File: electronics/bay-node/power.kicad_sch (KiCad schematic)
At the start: 26 parts, among them J1 24V IN, J2 24V OUT, Q1 SUD50P06-15, U1 TPS54360BDDAR, U2 AMS1117-3.3

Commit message: BOM: bulk hardware prices, JLC PCBA type per board
- hardware at bulk prices (T-nuts, screws, heat-set inserts, corner
  brackets), generic USB-C panel extensions; drop the label tape (the
  printed bay_label fills the drawer recess); heat-set inserts for camera
  pods only where a camera hangs
- catalog: standard_only flag (ESP32-S3-MINI-1, WS2812B-2020 cannot be
  placed with JLC Economic PCBA); bom.py prices Standard PCBA for the
  bay node and Economic for the power hub
- electrolytics moved to the Economic-capable LCSC listings of the same
  parts (C3352, C3358); PCB footprint fields synced, ERC/DRC/parity clean
- docs: JLC assembly notes (no Basic drop-ins for the extended parts)

Total ~EUR 927 -> ~EUR 828 (EUR 66 -> 59 per bay).

Co-Authored-By: Claude Opus 5.5 <noreply@anthropic.com>
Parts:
- C1: LCSC C72480 -> C3352; Manufacturer ROQANG -> Honor Elec
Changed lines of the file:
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@@
 			)
 		)
-		(property "Manufacturer" "ROQANG"
+		(property "Manufacturer" "Honor Elec"
 			(at 229.87 49.53 0)
 			(effects
@@
 			)
 		)
-		(property "LCSC" "C72480"
+		(property "LCSC" "C3352"
 			(at 229.87 49.53 0)
 			(effects

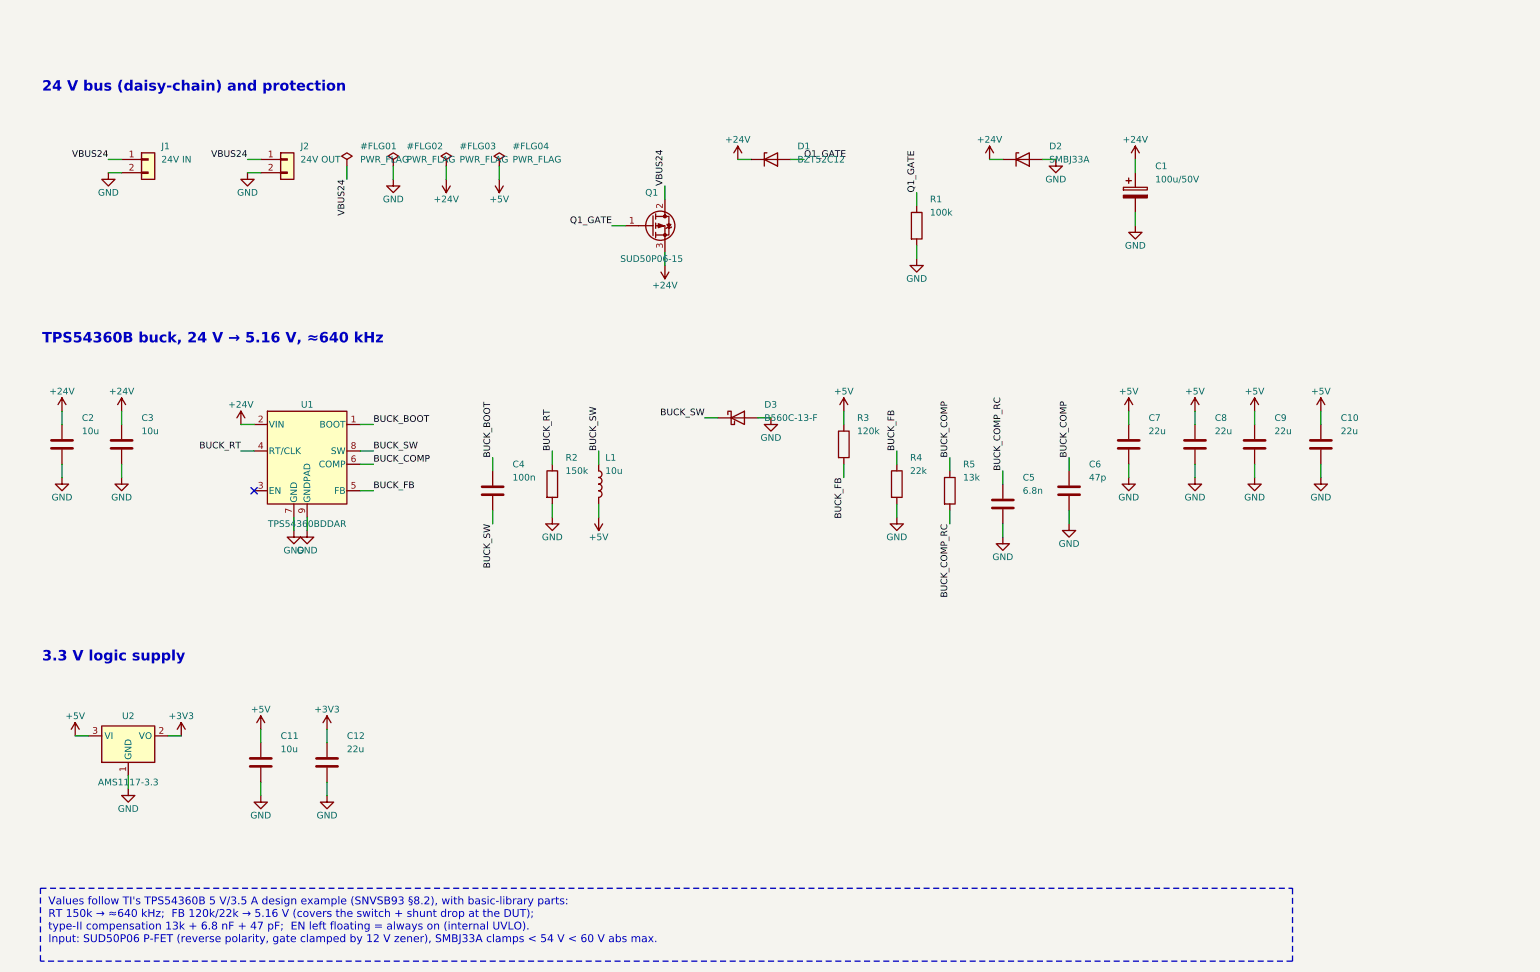
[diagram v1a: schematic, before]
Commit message: Schematics: draw real wires and an overview block diagram
The generator used to connect every pin through a net label only. Now,
in each block, the part with the most pins is the anchor and the
two-pin parts that share a signal with one of its side pins hang off
that pin on a real wire; parts chained behind them (R -> C -> GND)
stack underneath, and anchor-less blocks (pull-ups, reset/boot
buttons) are adopted by the anchor they connect to. Power symbols on
side pins point outward; power-flag references are hidden.

The root sheet becomes a block diagram: the supply rails each sheet
uses across the top, and one lane per pair of sheets listing the
signals they share.

Every wired net still carries one label, so net names, ERC (0) and the
PCB's schematic parity (0) are unchanged; the routed PCBs are untouched.

Co-Authored-By: Claude Opus 5.5 <noreply@anthropic.com>
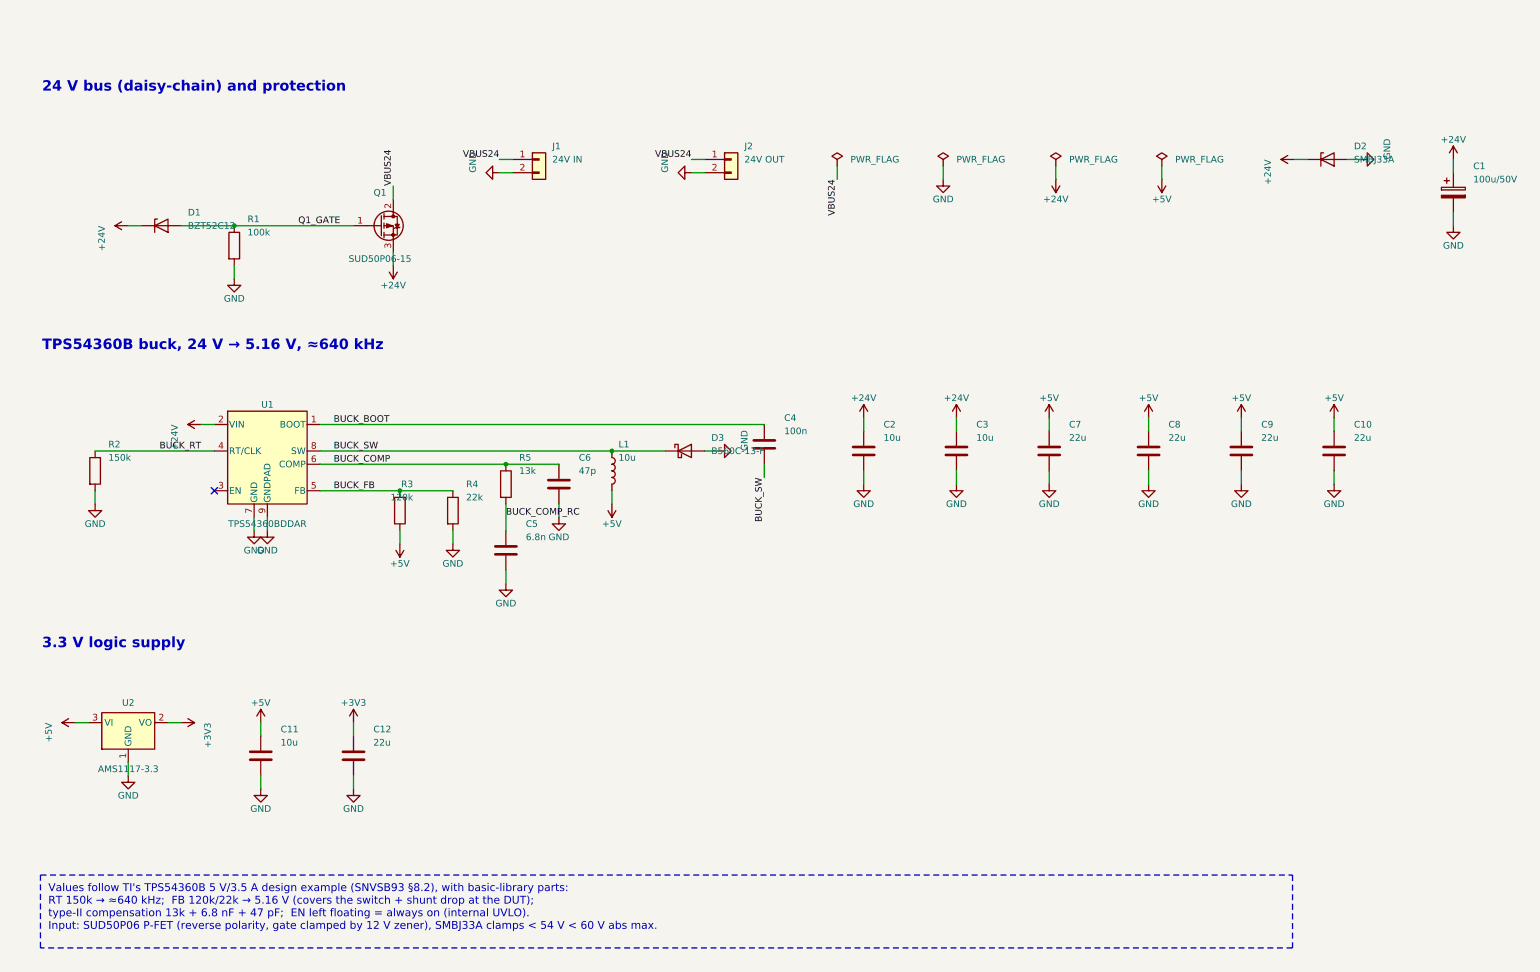
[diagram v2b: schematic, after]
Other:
- moved on the sheet: C1, C10, C11, C12, C2, C3, C4, C5, C6, C7, C8, C9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

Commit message: Boards v0.2: LMR51635 buck, JST PH, drawn schematics, thermal reliefs
Addresses Fabio's review of v0.1.

Bay node (rev 0.2):
- 5 V buck: LMR51635YDDCR (60 V, 3.5 A, synchronous, 1.1 MHz) with a
  3.3 uH FXL0630, 3 x 22 uF out, 2 x 10 uF + 100 nF in, FB 120k/22k
  (5.16 V), EN 1M/100k UVLO (13.5 V on, 10.8 V off). Replaces the
  TPS54360B, its Schottky and compensation network. CIN straddles the
  VIN/GND pins on solid top-side islands with vias to In1 (TI SLUSF64B).
- 24 V in/out on JST PH (carrier notches resized, rack.yaml pwr_y).
- Power nets named along the path: 24V_BUS -> +24V -> +5V -> DUT_5V_SW
  -> shunt -> DUT_5V; the INA226 visibly runs from +3V3.
- Stackup S+GND / GND / PWR / S+GND: In2 carries +5V, +3V3 under the
  ESP32 and a protected 24 V bus strip. Outer GND pours kept (without
  them Freerouting left ~25 connections unrouted).

Power hub (rev 0.2): JST VH input instead of the screw terminal, JST PH
row outputs, eFuse limit 1.6 A (RILIM 7.5k) to protect the 2 A contacts.

Generator:
- eda.py: drawn schematic mode (sch= placement, Sheet.wire/tag/frame,
  rotated/mirrored symbols, automatic junctions, per-island labels and
  checks that no wire touches another net); all seven sheets redrawn.
- pcbgen.py: thermal reliefs on every pour (+ <board>.kicad_dru for
  single spokes on fine pitch), configurable inner layers, per-zone
  deferral, fixed vias, DRC-driven fix-up for isolated GND pads.
- JLC CPL fix for the LMR51635 (270 deg); BOM, cables, viewer, docs.

ERC 0, DRC 0 copper errors, 0 unconnected, schematic parity 0 on both.

Co-Authored-By: Claude Opus 5.5 <noreply@anthropic.com>
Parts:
- removed C10: 22u, Capacitor_SMD:C_1206_3216Metric, symbol Device:C
- removed C6: 47p, Capacitor_SMD:C_0603_1608Metric, symbol Device:C
- removed D3: B560C-13-F, Diode_SMD:D_SMC, symbol Device:D_Schottky
- C5: value 6.8n -> 100n; LCSC C1631 -> C14663; MPN 0603B682K500NT -> CC0603KRX7R9BB104; Manufacturer FH (Guangdong Fenghua Advanced Tech) -> YAGEO
- J1, J2: footprint Connector_JST:JST_VH_S2P-VH_1x02_P3.96mm_Horizontal -> Connector_JST:JST_PH_S2B-PH-K_1x02_P2.00mm_Horizontal; LCSC C160355 -> C173752; MPN S2P-VH(LF)(SN) -> S2B-PH-K-S(LF)(SN)
- L1: value 10u -> 3.3u; footprint Inductor_SMD:L_Changjiang_FXL1040 -> Inductor_SMD:L_Changjiang_FXL0630; LCSC C475915 -> C167219; MPN FXL1040-100-M -> FXL0630-3R3-M
- R2: value 150k -> 1M; LCSC C22807 -> C22935; MPN 0603WAF1503T5E -> 0603WAF1004T5E
- R3: value 120k -> 100k; LCSC C25808 -> C25803; MPN 0603WAF1203T5E -> 0603WAF1003T5E
- R4: value 22k -> 120k; LCSC C31850 -> C25808; MPN 0603WAF2202T5E -> 0603WAF1203T5E
- R5: value 13k -> 22k; LCSC C22797 -> C31850; MPN 0603WAF1302T5E -> 0603WAF2202T5E
- U1: value TPS54360BDDAR -> LMR51635YDDCR; footprint Package_SO:TI_SO-PowerPAD-8_ThermalVias -> Package_TO_SOT_SMD:TSOT-23-6; symbol Regulator_Switching:TPS54360DDA -> bench:LMR51635; Alternative (none) -> LMR51635YFDDCR (C44750836): same, forced PWM, no spread spe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; LCSC C524806 -> C45262770; MPN TPS54360BDDAR -> LMR51635YDDCR
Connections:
- net +24V: now also C4.1, R2.1, U1.3 (VIN); no longer U1.2 (VIN)
- net +5V: now also R4.1; no longer R3.1
- net BUCK_FB: now also R4.2, R5.1, U1.1 (FB); no longer R3.2, R4.1, U1.5 (FB)
- net BUCK_SW: now also C5.2, U1.5 (SW); no longer C4.2, U1.8 (SW)
- net GND: now also C4.2, R3.2, R5.2, U1.4 (GND); no longer C5.2, R2.2, R4.2, U1.7 (GND), U1.9 (GNDPAD)
- removed net BUCK_BOOT: C4.1, U1.1 (BOOT)
- net BUCK_COMP renamed BUCK_CB
- net BUCK_CB: now also C5.1; no longer R5.1
- removed net BUCK_COMP_RC: C5.1, R5.2
- removed net BUCK_RT: R2.1, U1.4 (RT/CLK)
- net VBUS24 renamed 24V_BUS
- new net BUCK_EN: R2.2, R3.1, U1.2 (EN)
- no-connect marks 1 -> 0
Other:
- note added: "24 V bus in / out (daisy chain, JST PH) and input protection"
- note added: "5 V buck: LMR51635, synchronous, 1.1 MHz, 3.5 A (TI SLUSF64B typical application)"
- note removed: "24 V bus (daisy-chain) and protection"
- note removed: "TPS54360B buck, 24 V → 5.16 V, ≈640 kHz"
- moved on the sheet: C1, C11, C12, C2, C3, C4, C5, C7, C8, C9, D1, D2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

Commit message: Bay node v0.4: In2 power only, re-placed, SMD JST PH, new GPIO map
Fabio's second round: signals / GND / power / signals.  With no signal
on In2, v0.3's placement left 13-18 connections unrouted, mostly GPIOs
leaving the module's left column for the right half.  Connectors and
module stay put; the DUT power block moves to the top right, LDO and
buttons to the top left, the muxes under the module, and each GPIO sits
on the module edge facing its destination (firmware devicetree, README
pin table and docs follow; check_pinmap.py passes).

pcbgen: fanout_nets gives every GND/supply pin its own locked via to
its plane before routing.  USB HS pairs redrawn for the new geometry
(J3 -> J4 skew 0.1 mm).  J1/J2/J5/J6 are now S*B-PH-SM4-TB, placed by
JLC (24 V and GND on solid islands with 4 vias each); UART test pads on
the bottom side.  J5 is a JST PH 6 (Fabio: SH too small).

ERC 0, DRC 0 errors / 0 warnings / 0 unconnected, parity 0 (Konnect).

Co-Authored-By: Claude Opus 5.5 <noreply@anthropic.com>
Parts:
- J1, J2: footprint Connector_JST:JST_PH_S2B-PH-K_1x02_P2.00mm_Horizontal -> Connector_JST:JST_PH_S2B-PH-SM4-TB_1x02-1MP_P2.00mm_Horizontal; LCSC C173752 -> C295747; MPN S2B-PH-K-S(LF)(SN) -> S2B-PH-SM4-TB(LF)(SN)
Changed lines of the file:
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@@
 	(title_block
 		(title "Bay node — 24 V input, 5 V buck, 3.3 V LDO")
-		(rev "0.3")
+		(rev "0.4")
 		(company "hw-testing-rack")
 		(comment 1 "ESP32-S3 USB/IP host for one bay of the hw-testing-rack shelf")
@@
 			)
 		)
-		(property "Footprint" "Connector_JST:JST_PH_S2B-PH-K_1x02_P2.00mm_Horizontal"
+		(property "Footprint" "Connector_JST:JST_PH_S2B-PH-SM4-TB_1x02-1MP_P2.00mm_Horizontal"
 			(at 25.4 30.48 0)
 			(effects
@@
 			)
 		)
-		(property "Description" "JST PH 2-pin, side entry, 2 A"
+		(property "Description" "JST PH 2-pin, side entry, SMD, 2 A"
 			(at 25.4 30.48 0)
 			(effects
@@
 			)
 		)
-		(property "MPN" "S2B-PH-K-S(LF)(SN)"
+		(property "MPN" "S2B-PH-SM4-TB(LF)(SN)"
 			(at 25.4 30.48 0)
 			(effects
@@
 			)
 		)
-		(property "LCSC" "C173752"
+		(property "LCSC" "C295747"
 			(at 25.4 30.48 0)
 			(effects
@@
 			)
 		)
-		(property "Footprint" "Connector_JST:JST_PH_S2B-PH-K_1x02_P2.00mm_Horizontal"
+		(property "Footprint" "Connector_JST:JST_PH_S2B-PH-SM4-TB_1x02-1MP_P2.00mm_Horizontal"
 			(at 25.4 50.8 0)
 			(effects
@@
 			)
 		)
-		(property "Description" "JST PH 2-pin, side entry, 2 A"
+		(property "Description" "JST PH 2-pin, side entry, SMD, 2 A"
 			(at 25.4 50.8 0)
 			(effects
@@
 			)
 		)
-		(property "MPN" "S2B-PH-K-S(LF)(SN)"
+		(property "MPN" "S2B-PH-SM4-TB(LF)(SN)"
 			(at 25.4 50.8 0)
 			(effects
@@
 			)
 		)
-		(property "LCSC" "C173752"
+		(property "LCSC" "C295747"
 			(at 25.4 50.8 0)
 			(effects
